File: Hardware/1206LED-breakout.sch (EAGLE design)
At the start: 5 parts

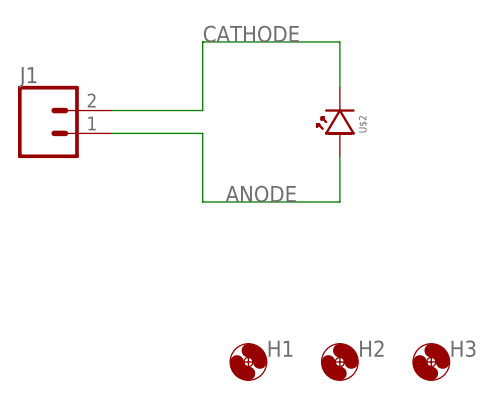
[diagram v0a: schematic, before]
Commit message: Updated breakouts and main board, schematic v0.1 updates
Updated schematic for main unit to v0.1, incorporating updates from testing of v0.0 unit
Minor updates to breakout boards, adding passives and updating components
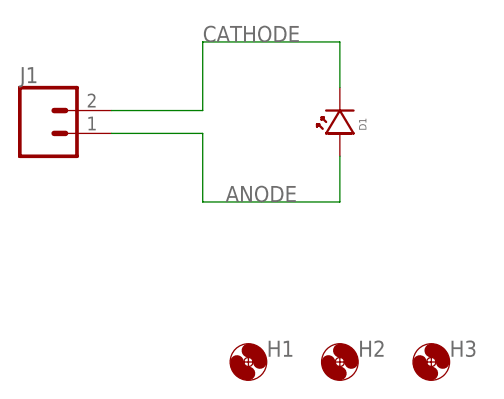
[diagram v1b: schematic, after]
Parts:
- removed U$2: 1206-LED, bschulz:1206-LED
- added D1: LED1206, bschulz:LED1206
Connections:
- net ANODE: now also D1.ANODE; no longer U$2.ANODE
- net CATHODE: now also D1.CATHODE; no longer U$2.CATHODE
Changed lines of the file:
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@@
 <?xml version="1.0" encoding="utf-8"?>
 <!DOCTYPE eagle SYSTEM "eagle.dtd">
-<eagle version="9.2.0">
+<eagle version="9.1.3">
 <drawing>
 <settings>
@@
 <layers>
 <layer number="1" name="Top" color="4" fill="1" visible="no" active="no"/>
+<layer number="2" name="Route2" color="1" fill="3" visible="no" active="no"/>
+<layer number="3" name="Route3" color="4" fill="3" visible="no" active="no"/>
+<layer number="4" name="Route4" color="1" fill="4" visible="no" active="no"/>
+<layer number="5" name="Route5" color="4" fill="4" visible="no" active="no"/>
+<layer number="6" name="Route6" color="1" fill="8" visible="no" active="no"/>
+<layer number="7" name="Route7" color="4" fill="8" visible="no" active="no"/>
+<layer number="8" name="Route8" color="1" fill="2" visible="no" active="no"/>
+<layer number="9" name="Route9" color="4" fill="2" visible="no" active="no"/>
+<layer number="10" name="Route10" color="1" fill="7" visible="no" active="no"/>
+<layer number="11" name="Route11" color="4" fill="7" visible="no" active="no"/>
+<layer number="12" name="Route12" color="1" fill="5" visible="no" active="no"/>
+<layer number="13" name="Route13" color="4" fill="5" visible="no" active="no"/>
+<layer number="14" name="Route14" color="1" fill="6" visible="no" active="no"/>
+<layer number="15" name="Route15" color="4" fill="6" visible="no" active="no"/>
 <layer number="16" name="Bottom" color="1" fill="1" visible="no" active="no"/>
 <layer number="17" name="Pads" color="2" fill="1" visible="no" active="no"/>
@@
 <part name="H2" library="bschulz" deviceset="MOUNTING_HOLE" device="2_NP"/>
 <part name="H3" library="bschulz" deviceset="MOUNTING_HOLE" device="2_NP"/>
-<part name="U$2" library="bschulz" deviceset="1206-LED" device=""/>
+<part name="D1" library="bschulz" deviceset="LED" device="1206"/>
 <part name="J1" library="bschulz" deviceset="CONN_02" device="1X02_NO_SILK"/>
 </parts>
@@
 <attribute name="VALUE" x="159.512" y="86.4362" size="1.778" layer="96"/>
 </instance>
-<instance part="U$2" gate="G$1" x="147.32" y="114.3">
+<instance part="D1" gate="G$1" x="147.32" y="114.3">
 <attribute name="NAME" x="149.86" y="115.316" size="0.8128" layer="95" font="vector" ratio="15" rot="R90" align="center"/>
 </instance>
@@
 <net name="ANODE" class="0">
 <segment>
-<pinref part="U$2" gate="G$1" pin="ANODE"/>
+<pinref part="D1" gate="G$1" pin="ANODE"/>
 <wire x1="147.32" y1="111.76" x2="147.32" y2="106.68" width="0.1524" layer="91"/>
 <wire x1="147.32" y1="106.68" x2="132.08" y2="106.68" width="0.1524" layer="91"/>
@@
 <net name="CATHODE" class="0">
 <segment>
-<pinref part="U$2" gate="G$1" pin="CATHODE"/>
+<pinref part="D1" gate="G$1" pin="CATHODE"/>
 <wire x1="147.32" y1="119.38" x2="147.32" y2="124.46" width="0.1524" layer="91"/>
 <wire x1="147.32" y1="124.46" x2="132.08" y2="124.46" width="0.1524" layer="91"/>
